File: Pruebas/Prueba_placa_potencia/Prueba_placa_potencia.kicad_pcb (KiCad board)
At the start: 2 copper layers, 54 parts, among them J1 Conn_01x03_Pin, J2 Conn_01x03_Pin, J3 Screw_Terminal_01x02, J4 Screw_Terminal_01x02, J6 Conn_01x03_Pin, J7 LOAD+, J8 LOAD-, Q1 2N2222A, Q10 2N2222A, Q11 TIP142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

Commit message: Routing
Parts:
- moved R10 8.18 mm to (21.0, 27.3), turned to 0 degrees
- moved R16 8.11 mm to (75.5, 27.0), turned to 0 degrees
- moved Q2 7.32 mm to (27.8, 32.8), turned to 180 degrees
- moved R19 7.19 mm to (20.8, 74.1), turned to 0 degrees
- moved Q6 5.29 mm to (25.6, 79.5)
- moved Q4 4.92 mm to (80.3, 32.5)
- moved Q9 1.41 mm to (48.1, 79.8)
- moved R20 1.41 mm to (26.7, 90.6)
- moved R21 1.41 mm to (21.9, 90.6)
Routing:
- net Net-(Q1-Pad3): track 0.00 -> 267.8 mm
- net SRC+: track 0.00 -> 232.0 mm
- net /B: track 0.00 -> 106.5 mm
- net Net-(Q7-E): track 39.9 -> 78.3 mm
- net Net-(Q11-E): track 37.7 -> 68.4 mm
- net Net-(Q9-B): track 31.3 -> 27.6 mm
- net Net-(Q11-B): track 31.0 -> 28.2 mm
- net Net-(Q3-B): track 30.6 -> 28.6 mm
- net Net-(Q9-E): track 37.3 -> 37.8 mm

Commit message: Routing complete
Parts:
- C2, C3: footprint Capacitor_THT:CP_Radial_D5.0mm_P2.00mm -> Capacitor_THT:CP_Radial_D5.0mm_P2.50mm
- Q1, Q10, Q2, Q4, Q6, Q8: footprint Package_TO_SOT_THT:TO-92_Inline -> Package_TO_SOT_THT:TO-92L_Inline_Wide
- moved Q1 84.3 mm to (74.8, 114.8), turned to 90 degrees
- moved D2 74.6 mm to (82.3, 118.9), turned to -90 degrees
- moved R28 65.5 mm to (115.0, 110.3), turned to 180 degrees
- moved J4 61.5 mm to (89.0, 162.9)
- moved J8 58.1 mm to (104.6, 162.8)
- moved Q10 57.5 mm to (69.8, 161.8), turned to 90 degrees
- moved J7 56.0 mm to (117.8, 162.8)
- moved R12 55.3 mm to (92.6, 132.0), turned to -90 degrees
- moved R11 54.2 mm to (89.5, 132.0), turned to -90 degrees
- moved C1 53.5 mm to (98.1, 122.5)
- moved J6 51.6 mm to (94.9, 127.9), turned to -90 degrees
- moved C4 47.5 mm to (105.3, 122.2), turned to 90 degrees
- moved R14 47.4 mm to (95.7, 132.0), turned to -90 degrees
- moved U1 46.3 mm to (99.1, 129.1)
- moved R27 45.7 mm to (67.6, 140.3), turned to 0 degrees
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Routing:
- net /E: track 0.00 -> 455.1 mm
- net /B: track 106.5 -> 344.7 mm
- net Net-(Q1-Pad3): track 267.8 -> 495.7 mm
- net Net-(J2-Pin_2): track 0.00 -> 55.9 mm
- net SRC+: track 232.0 -> 282.8 mm
- net VCC: track 0.00 -> 38.5 mm
- net Net-(D2-A): track 0.00 -> 30.7 mm
- net Net-(U1A--): track 0.00 -> 27.1 mm
- net Net-(Q5-B): track 31.8 -> 58.8 mm
- net Net-(D3-K): track 0.00 -> 24.4 mm
- net Net-(Q9-B): track 27.6 -> 50.7 mm
- net Net-(J6-Pin_3): track 0.00 -> 22.5 mm
- net Net-(Q5-E): track 36.9 -> 57.0 mm
- net Net-(J1-Pin_3): track 0.00 -> 13.5 mm
- net Net-(Q7-E): track 78.3 -> 66.2 mm
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- added copper zone on B.Cu, net GND
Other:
- board outline added: 95.3 x 150.9 mm

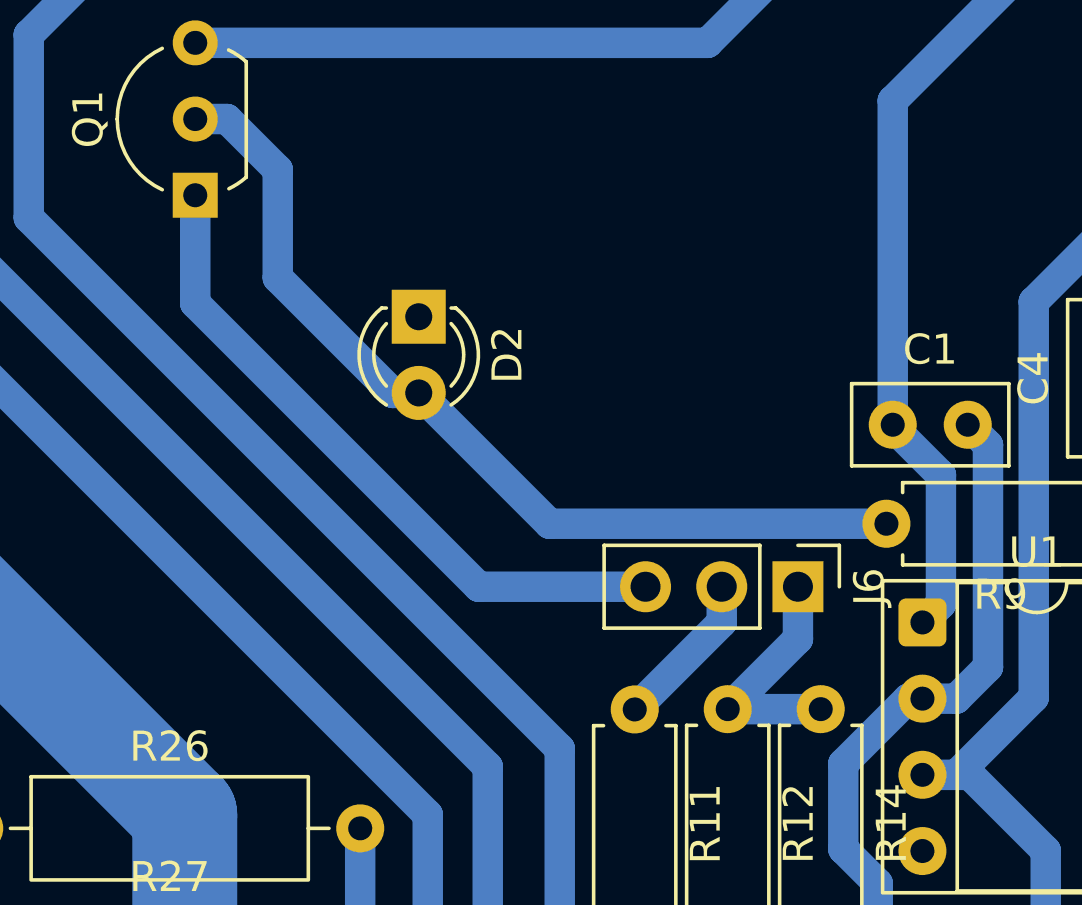
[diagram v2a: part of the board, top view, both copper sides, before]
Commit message: Correct jumper connections
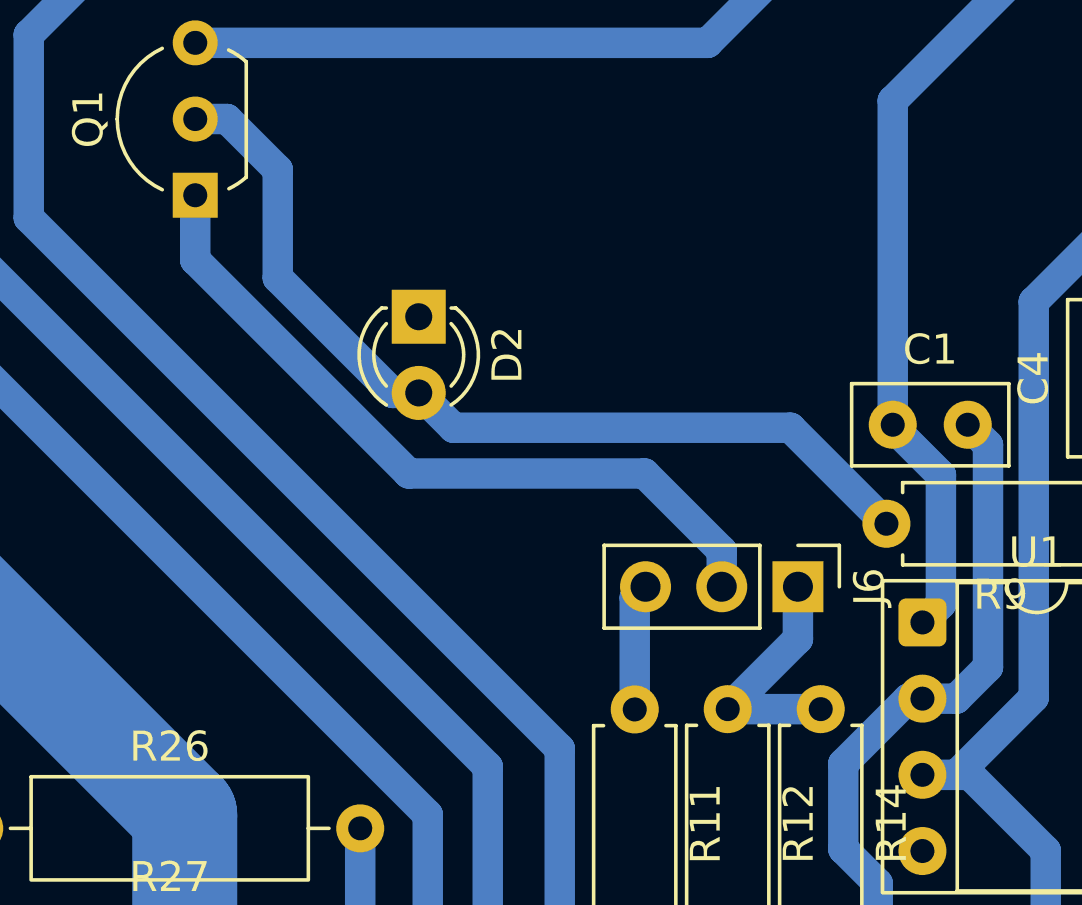
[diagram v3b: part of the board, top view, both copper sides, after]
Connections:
- Q1 pad 1: Net-(J6-Pin_3) -> Net-(J6-Pin_2)
- R11 pad 1: Net-(J6-Pin_2) -> Net-(J6-Pin_3)
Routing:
- net Net-(J6-Pin_2): track 5.29 -> 24.9 mm
- net Net-(J6-Pin_3): track 22.5 -> 4.24 mm
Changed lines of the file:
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@@
 			(layers "*.Cu" "*.Mask")
 			(remove_unused_layers no)
-			(net 16 "Net-(J6-Pin_2)")
+			(net 15 "Net-(J6-Pin_3)")
 			(pintype "passive")
 		)
@@
 		(tags "TO-247-3 Vertical RM 5.45mm")
 		(property "Reference" "Q3"
-			(at 5.45 -3.28 270)
+			(at 5.45 -3.28 90)
 			(layer "F.SilkS")
 			(effects
@@
 		)
 		(property "Value" "TIP142"
-			(at 5.45 3.65 270)
+			(at 5.45 3.65 90)
 			(layer "F.Fab")
 			(effects
@@
 		)
 		(property "Datasheet" "~"
-			(at 0 0 270)
+			(at 0 0 90)
 			(layer "F.Fab")
 			(hide yes)
@@
 		)
 		(property "Description" "NPN Darlington transistor, base/collector/emitter"
-			(at 0 0 270)
+			(at 0 0 90)
 			(layer "F.Fab")
 			(hide yes)
@@
 		)
 		(fp_text user "${REFERENCE}"
-			(at 5.45 0.19 270)
+			(at 5.45 0.19 90)
 			(layer "F.Fab")
 			(effects
@@
 			(layers "*.Cu" "*.Mask")
 			(remove_unused_layers no)
-			(net 15 "Net-(J6-Pin_3)")
+			(net 16 "Net-(J6-Pin_2)")
 			(pintype "passive")
 		)
@@
 	)
 	(segment
-		(start 86.66 125.8)
+		(start 97.89 125.8)
+		(end 94.69 122.6)
+		(width 1.016)
+		(layer "B.Cu")
+		(net 5)
+	)
+	(segment
+		(start 83.46 122.6)
 		(end 82.3 121.44)
 		(width 1.016)
@@
 	)
 	(segment
-		(start 97.89 125.8)
-		(end 86.66 125.8)
+		(start 77.6 117.6)
+		(end 77.6 113.99934)
 		(width 1.016)
 		(layer "B.Cu")
@@
 	)
 	(segment
-		(start 77.6 117.6)
-		(end 77.6 113.99934)
+		(start 94.69 122.6)
+		(end 83.46 122.6)
 		(width 1.016)
 		(layer "B.Cu")
@@
 	)
 	(segment
-		(start 84.3 127.9)
-		(end 74.85 118.45)
+		(start 89.5 128.26)
+		(end 89.86 127.9)
 		(width 1.016)
 		(layer "B.Cu")
@@
 	)
 	(segment
-		(start 89.86 127.9)
-		(end 84.3 127.9)
+		(start 89.5 131.99)
+		(end 89.5 128.26)
 		(width 1.016)
 		(layer "B.Cu")
@@
 	)
 	(segment
-		(start 74.85 118.45)
+		(start 89.827081 124.125)
+		(end 81.968324 124.125)
+		(width 1.016)
+		(layer "B.Cu")
+		(net 16)
+	)
+	(segment
+		(start 92.4 126.697919)
+		(end 89.827081 124.125)
+		(width 1.016)
+		(layer "B.Cu")
+		(net 16)
+	)
+	(segment
+		(start 74.85 117.006676)
 		(end 74.85 114.85)
 		(width 1.016)
 		(layer "B.Cu")
-		(net 15)
+		(net 16)
 	)
 	(segment
-		(start 92.4 129.09)
-		(end 89.5 131.99)
+		(start 81.968324 124.125)
+		(end 74.85 117.006676)
 		(width 1.016)
 		(layer "B.Cu")
@@
 	(segment
 		(start 92.4 127.9)
-		(end 92.4 129.09)
+		(end 92.4 126.697919)
 		(width 1.016)
 		(layer "B.Cu")
@@
 		(min_thickness 0.25)
 		(filled_areas_thickness no)
-		(fill yes
+		(fill
 			(thermal_gap 0.5)
 			(thermal_bridge_width 0.5)
